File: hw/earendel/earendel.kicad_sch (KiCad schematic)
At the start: 0 parts

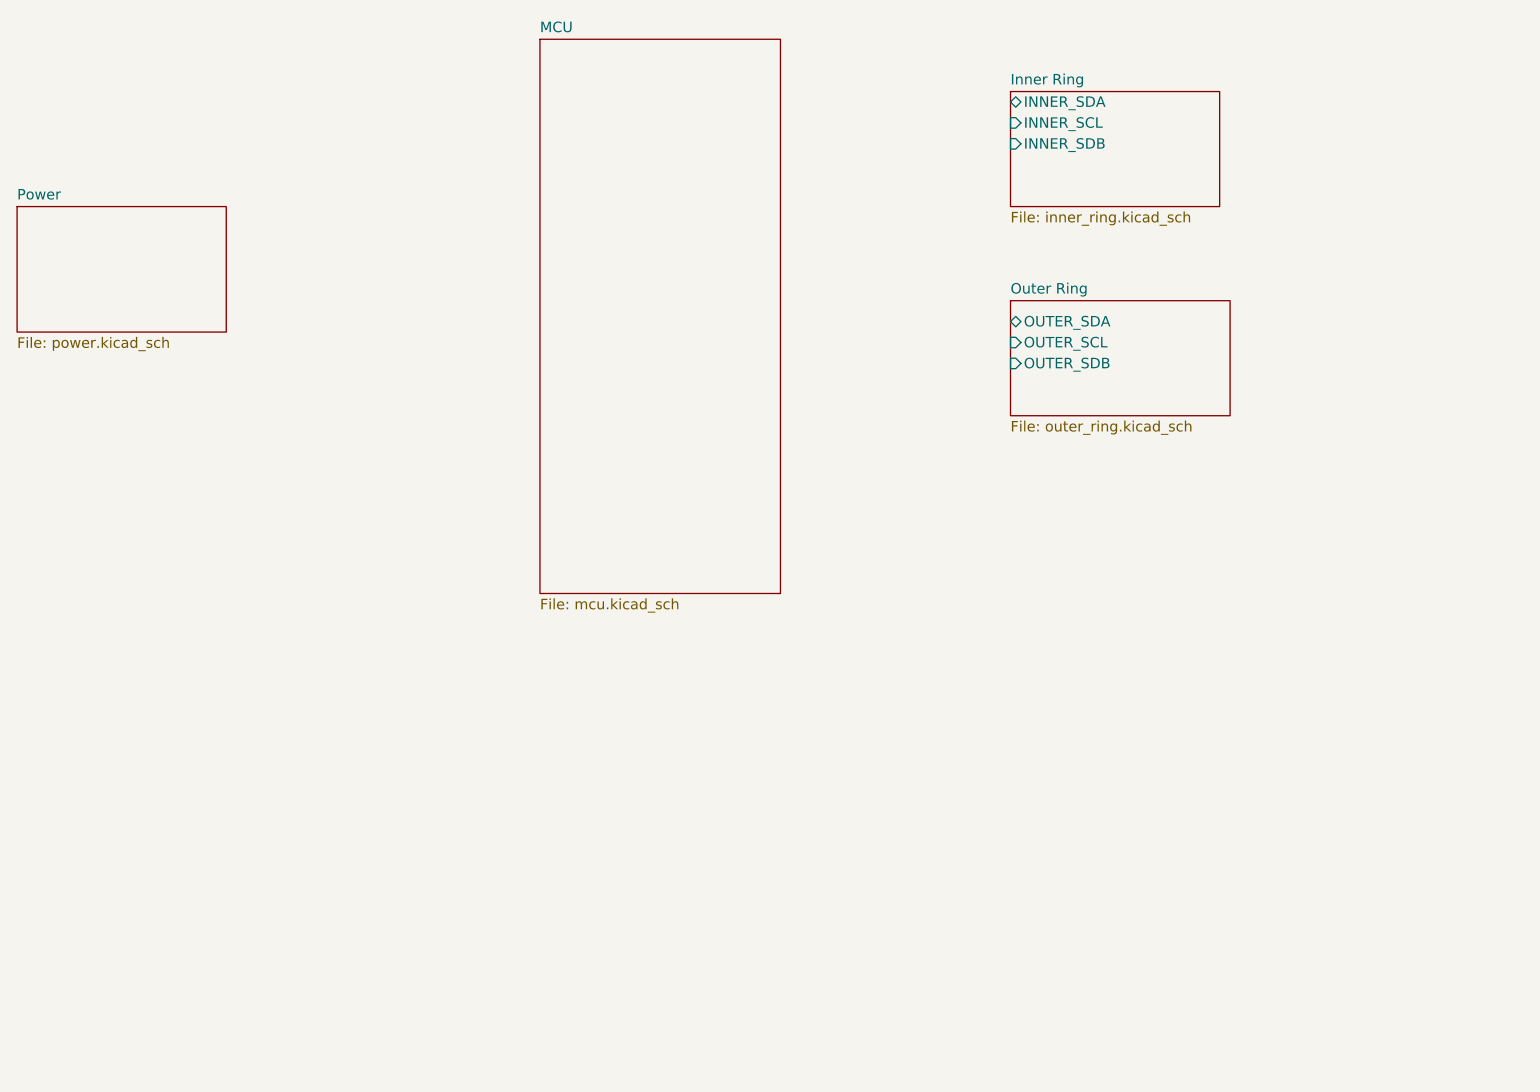
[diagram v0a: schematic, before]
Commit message: New blank kicad project, add esp32 mcu and initial usb connector
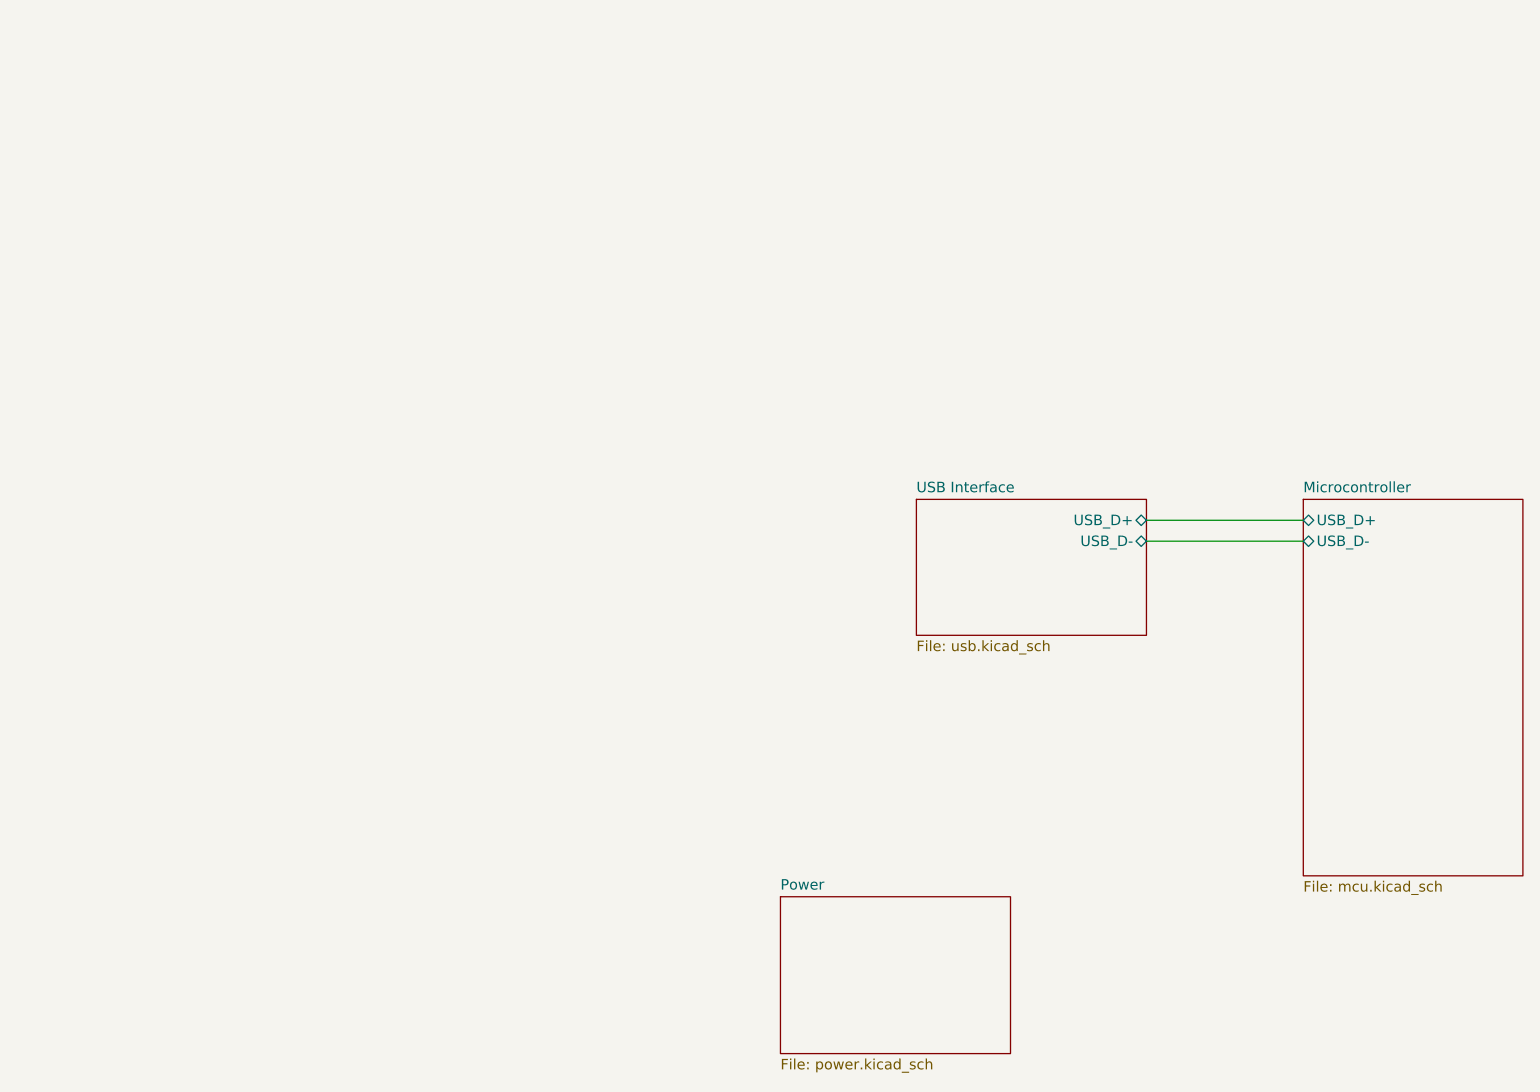
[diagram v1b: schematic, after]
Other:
- removed sheet Inner Ring
- removed sheet MCU
- removed sheet Outer Ring
- added sheet Microcontroller (mcu.kicad_sch)
- added sheet USB Interface (usb.kicad_sch)
- company: Aaron & Ryan Shappell -> Catlock
- title: Earendel Ring Light -> Earendel Microscope Ring Light
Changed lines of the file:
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@@
 (kicad_sch
-	(version 20231120)
+	(version 20260306)
 	(generator "eeschema")
-	(generator_version "8.0")
-	(paper "A4")
+	(generator_version "10.0")
+	(paper "A3")
 	(title_block
-		(title "Earendel Ring Light")
-		(date "2024-08-30")
-		(rev "Rev001")
-		(company "Aaron & Ryan Shappell")
+		(title "Earendel Microscope Ring Light")
+		(date "2026-09-27")
+		(rev "PRE")
+		(company "Catlock")
+	)
+	(wire
+		(pts
+			(xy 196.85 119.38) (xy 215.9 119.38)
+		)
+		(stroke
+			(width 0)
+			(type default)
+		)
+	)
+	(wire
+		(pts
+			(xy 196.85 116.84) (xy 215.9 116.84)
+		)
+		(stroke
+			(width 0)
+			(type default)
+		)
 	)
 	(sheet
-		(at 180.34 90.17)
-		(size 26.67 13.97)
+		(at 152.4 162.56)
+		(size 27.94 19.05)
+		(exclude_from_sim no)
+		(in_bom yes)
+		(on_board yes)
+		(dnp no)
 		(fields_autoplaced yes)
 		(stroke
@@
 		)
 		(fill
-			(color 0 0 0 0.0000)
-		)
-		(property "Sheetname" "Outer Ring"
-			(at 180.34 89.4584 0)
+			(color 0 0 0 0)
+		)
+		(property "Sheetname" "Power"
+			(at 152.4 161.8484 0)
+			(show_name no)
+			(do_not_autoplace no)
 			(effects
 				(font
@@
 			)
 		)
-		(property "Sheetfile" "outer_ring.kicad_sch"
-			(at 180.34 104.7246 0)
+		(property "Sheetfile" "power.kicad_sch"
+			(at 152.4 182.1946 0)
+			(show_name no)
+			(do_not_autoplace no)
 			(effects
 				(font
@@
 				)
 				(justify left top)
-			)
-		)
-		(pin "OUTER_SDA" bidirectional
-			(at 180.34 92.71 180)
-			(effects
-				(font
-					(size 1.27 1.27)
-				)
-				(justify left)
-			)
-		)
-		(pin "OUTER_SCL" input
-			(at 180.34 95.25 180)
-			(effects
-				(font
-					(size 1.27 1.27)
-				)
-				(justify left)
-			)
-		)
-		(pin "OUTER_SDB" input
-			(at 180.34 97.79 180)
-			(effects
-				(font
-					(size 1.27 1.27)
-				)
-				(justify left)
 			)
 		)
 		(instances
 			(project "earendel"
-				(path "/9f298bf9-d1b7-4300-ae61-070881d679f0"
-					(page "5")
+				(path "/7dbd9be6-8f9f-4eba-82d5-5a1751002bf1"
+					(page "4")
 				)
 			)
@@
 	)
 	(sheet
-		(at 123.19 58.42)
-		(size 29.21 67.31)
+		(at 168.91 114.3)
+		(size 27.94 16.51)
+		(exclude_from_sim no)
+		(in_bom yes)
+		(on_board yes)
+		(dnp no)
 		(fields_autoplaced yes)
 		(stroke
@@
 		)
 		(fill
-			(color 0 0 0 0.0000)
-		)
-		(property "Sheetname" "MCU"
-			(at 123.19 57.7084 0)
+			(color 0 0 0 0)
+		)
+		(property "Sheetname" "USB Interface"
+			(at 168.91 113.5884 0)
+			(show_name no)
+			(do_not_autoplace no)
 			(effects
 				(font
@@
 			)
 		)
-		(property "Sheetfile" "mcu.kicad_sch"
-			(at 123.19 126.3146 0)
+		(property "Sheetfile" "usb.kicad_sch"
+			(at 168.91 131.3946 0)
+			(show_name no)
+			(do_not_autoplace no)
 			(effects
 				(font
@@
 				)
 				(justify left top)
+			)
+		)
+		(pin "USB_D+" bidirectional
+			(at 196.85 116.84 0)
+			(effects
+				(font
+					(size 1.27 1.27)
+				)
+				(justify right)
+			)
+		)
+		(pin "USB_D-" bidirectional
+			(at 196.85 119.38 0)
+			(effects
+				(font
+					(size 1.27 1.27)
+				)
+				(justify right)
 			)
 		)
 		(instances
 			(project "earendel"
-				(path "/9f298bf9-d1b7-4300-ae61-070881d679f0"
-					(page "2")
+				(path "/7dbd9be6-8f9f-4eba-82d5-5a1751002bf1"
+					(page "3")
 				)
 			)
@@
 	)
 	(sheet
-		(at 180.34 64.77)
-		(size 25.4 13.97)
+		(at 215.9 114.3)
+		(size 26.67 45.72)
+		(exclude_from_sim no)
+		(in_bom yes)
+		(on_board yes)
+		(dnp no)
 		(fields_autoplaced yes)
 		(stroke
@@
 		)
 		(fill
-			(color 0 0 0 0.0000)
-		)
-		(property "Sheetname" "Inner Ring"
-			(at 180.34 64.0584 0)
+			(color 0 0 0 0)
+		)
+		(property "Sheetname" "Microcontroller"
+			(at 215.9 113.5884 0)
+			(show_name no)
+			(do_not_autoplace no)
 			(effects
 				(font
@@
 			)
 		)
-		(property "Sheetfile" "inner_ring.kicad_sch"
-			(at 180.34 79.3246 0)
+		(property "Sheetfile" "mcu.kicad_sch"
+			(at 215.9 160.6046 0)
+			(show_name no)
+			(do_not_autoplace no)
 			(effects
 				(font
@@
 			)
 		)
-		(pin "INNER_SCL" input
-			(at 180.34 68.58 180)
+		(pin "USB_D+" bidirectional
+			(at 215.9 116.84 180)
 			(effects
 				(font
@@
 			)
 		)
-		(pin "INNER_SDB" input
-			(at 180.34 71.12 180)
-			(effects
-				(font
-					(size 1.27 1.27)
-				)
-				(justify left)
-			)
-		)
-		(pin "INNER_SDA" bidirectional
-			(at 180.34 66.04 180)
+		(pin "USB_D-" bidirectional
+			(at 215.9 119.38 180)
 			(effects
 				(font
@@
 		(instances
 			(project "earendel"
-				(path "/9f298bf9-d1b7-4300-ae61-070881d679f0"
-					(page "4")
-				)
-			)
-		)
-	)
-	(sheet
-		(at 59.69 78.74)
-		(size 25.4 15.24)
-		(fields_autoplaced yes)
-		(stroke
-			(width 0.1524)
-			(type solid)
-		)
-		(fill
-			(color 0 0 0 0.0000)
-		)
-		(property "Sheetname" "Power"
-			(at 59.69 78.0284 0)
-			(effects
-				(font
-					(size 1.27 1.27)
-				)
-				(justify left bottom)
-			)
-		)
-		(property "Sheetfile" "power.kicad_sch"
-			(at 59.69 94.5646 0)
-			(effects
-				(font
-					(size 1.27 1.27)
-				)
-				(justify left top)
-			)
-		)
-		(instances
-			(project "earendel"
-				(path "/9f298bf9-d1b7-4300-ae61-070881d679f0"
-					(page "3")
+				(path "/7dbd9be6-8f9f-4eba-82d5-5a1751002bf1"
+					(page "2")
 				)
 			)
@@
 		)
 	)
+	(embedded_fonts no)
 )
